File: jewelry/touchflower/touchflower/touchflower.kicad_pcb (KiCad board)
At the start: 2 copper layers, 22 x 22 mm, 10 parts, among them J1 Conn_01x01, J2 Conn_01x01, J3 Conn_01x01, J4 Conn_01x01, U1 TPP223-BA6

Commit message: jewelry: Tested touchflower PCB for 2032
Works nicely, including using wires to make a batteryholder
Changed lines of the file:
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@@
     (mod_text_size 1 1)
     (mod_text_width 0.15)
-    (pad_size 2.5 2.5)
-    (pad_drill 2)
+    (pad_size 2 2)
+    (pad_drill 0.65)
     (pad_to_mask_clearance 0.2)
     (aux_axis_origin 0 0)
     (visible_elements FFFFFF7F)
     (pcbplotparams
-      (layerselection 0x010f0_ffffffff)
+      (layerselection 0x01000_7fffffff)
       (usegerberextensions false)
       (usegerberattributes false)
@@
       (padsonsilk false)
       (subtractmaskfromsilk false)
-      (outputformat 1)
+      (outputformat 5)
       (mirror false)
-      (drillshape 0)
+      (drillshape 1)
       (scaleselection 1)
-      (outputdirectory ./gerbers/))
+      (outputdirectory ./out))
   )
   (net 0 "")
@@
       (effects (font (size 1 1) (thickness 0.15)))
     )
-    (pad 1 thru_hole rect (at 0 0) (size 1 1) (drill 0.65) (layers *.Cu *.Mask)
+    (pad 1 thru_hole rect (at 0 0) (size 2 2) (drill 0.65) (layers *.Cu *.Mask)
       (net 3 VDD))
     (model ${KISYS3DMOD}/Pin_Headers.3dshapes/Pin_Header_Straight_1x01_Pitch1.27mm.wrl
@@
     (fp_line (start 1.05 -0.635) (end 1.05 0.635) (layer F.Fab) (width 0.1))
     (fp_line (start -0.525 -0.635) (end 1.05 -0.635) (layer F.Fab) (width 0.1))
-    (pad 1 thru_hole rect (at 0 0) (size 1 1) (drill 0.65) (layers *.Cu *.Mask)
+    (pad 1 thru_hole rect (at 0 0) (size 2 2) (drill 0.65) (layers *.Cu *.Mask)
       (net 1 GND))
     (model ${KISYS3DMOD}/Pin_Headers.3dshapes/Pin_Header_Straight_1x01_Pitch1.27mm.wrl
@@
       (effects (font (size 1 1) (thickness 0.15)))
     )
-    (pad 1 thru_hole rect (at 0 0) (size 1 1) (drill 0.65) (layers *.Cu *.Mask)
+    (pad 1 thru_hole rect (at 0 0) (size 2 2) (drill 0.65) (layers *.Cu *.Mask)
       (net 5 /sensor))
     (model ${KISYS3DMOD}/Pin_Headers.3dshapes/Pin_Header_Straight_1x01_Pitch1.27mm.wrl
@@
     (fp_line (start 1.05 -0.635) (end 1.05 0.635) (layer F.Fab) (width 0.1))
     (fp_line (start -0.525 -0.635) (end 1.05 -0.635) (layer F.Fab) (width 0.1))
-    (pad 1 thru_hole rect (at 0 0) (size 1 1) (drill 0.65) (layers *.Cu *.Mask)
+    (pad 1 thru_hole rect (at 0 0) (size 2 2) (drill 0.65) (layers *.Cu *.Mask)
       (net 6 /out))
     (model ${KISYS3DMOD}/Pin_Headers.3dshapes/Pin_Header_Straight_1x01_Pitch1.27mm.wrl
@@
   (segment (start 0.08 2.54) (end 0.08 1.985) (width 0.4) (layer F.Cu) (net 1))
   (segment (start 0 -2.54) (end 0 -2.54) (width 0.4) (layer F.Cu) (net 1))
-  (via (at 0 -2.54) (size 1.2) (drill 0.8) (layers F.Cu B.Cu) (net 1))
+  (via (at 0 -2.54) (size 1.5) (drill 0.8) (layers F.Cu B.Cu) (net 1))
   (segment (start 0.08 2.794) (end 0.08 2.54) (width 0.4) (layer F.Cu) (net 1))
-  (via (at 0.08 2.794) (size 1.2) (drill 0.8) (layers F.Cu B.Cu) (net 1))
+  (via (at 0.08 2.794) (size 1.5) (drill 0.8) (layers F.Cu B.Cu) (net 1))
   (segment (start 6.885 5.08) (end 7.05001 5.24501) (width 0.4) (layer F.Cu) (net 2))
   (segment (start 6.43 5.08) (end 6.885 5.08) (width 0.4) (layer F.Cu) (net 2))

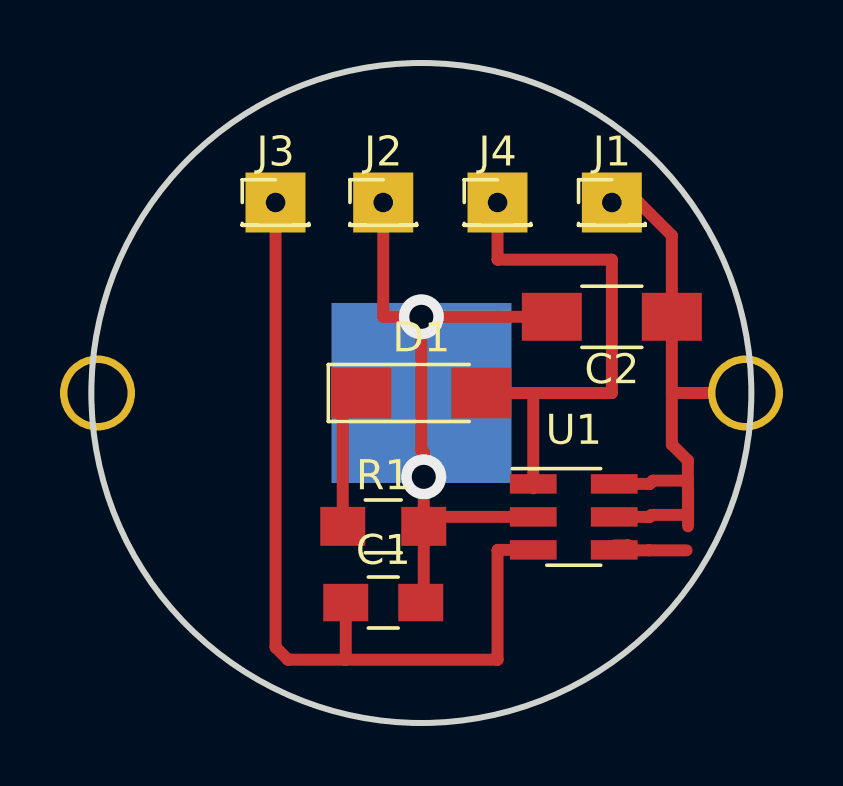
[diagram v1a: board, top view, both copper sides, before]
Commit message: jewelry: Miniaturize touchflower
Dropped battery holder and allow connection points on all sides
Down to <11mm diameter with 1206/0805.
Sub 10mm possible 0805/0603, should still be millable
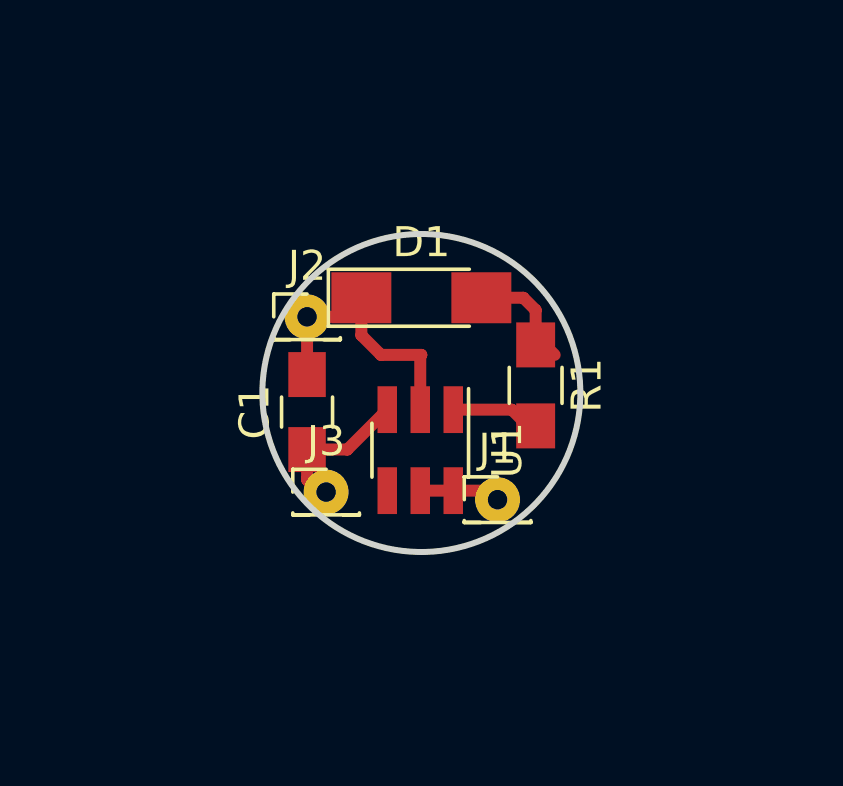
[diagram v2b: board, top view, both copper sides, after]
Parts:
- removed BT1: Battery_Cell, touchflower:BK-913
- removed C2: CP, Capacitors_SMD:C_1206_HandSoldering
- removed J4: Conn_01x01, Pin_Headers:Pin_Header_Straight_1x01_Pitch1.27mm
- moved J1 10.6 mm to (2.54, 3.56)
- moved J3 9.80 mm to (-3.17, 3.30)
- moved R1 6.92 mm to (3.81, -0.25), turned to 270 degrees
- moved C1 6.84 mm to (-3.81, 0.64), turned to 90 degrees
- moved U1 5.58 mm to (-0.04, 1.91), turned to 270 degrees
- moved J2 4.58 mm to (-3.81, -2.54)
- moved D1 3.17 mm to (0.00, -3.17)
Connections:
- D1 pad 1: Net-(D1-Pad1) -> GND
- D1 pad 2: /out -> Net-(D1-Pad2)
- R1 pad 1: Net-(D1-Pad1) -> Net-(D1-Pad2)
- R1 pad 2: GND -> /out
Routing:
- net /sensor: track 29.2 -> 4.78 mm
- net VDD: track 19.5 -> 3.27 mm
- net /out: track 17.7 -> 3.08 mm
- net GND: track 23.6 -> 9.36 mm, vias 2 -> 0
- net Net-(D1-Pad1): track 4.70 -> 0.00 mm
- net Net-(D1-Pad2): track 0.00 -> 4.29 mm
- net Net-(U1-Pad4): track 2.48 -> 0.00 mm
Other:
- board size 22 x 22 mm -> 10.6 x 10.6 mm
